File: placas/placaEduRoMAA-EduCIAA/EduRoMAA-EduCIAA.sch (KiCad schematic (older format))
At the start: 78 parts, among them J1 DC_IN, J2 Motor_Izq, J3 Motor_Der, J4 Bluetooth, J5 Sonar, J6 DC_OUT, J7 DC_IN, Q1 BC548, Q2 BC548, Q3 BC548, Q4 BC548, Q5 BC548, SW1 SW_Push, SW2 SW_Push, U1 TCRT5000, U2 TCRT5000, U3 TCST1103, U4 LM393, U5 TCST1103, U6 L293D, U7 IRF7105, U8 IRF7105

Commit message: Reorganizo esquematico y uno librerias
Reorganización general, elimino net repetidas y uno las librerias en una sola
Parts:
- BZ1: symbol EduRoMAA-EduCIAA-rescue:Buzzer-ROBUC_v00_D-ROBUC_v02_EduCiAA-rescue -> EduRoMAA-EduCIAA:Buzzer
- C1, C10, C2, C3, C8, C9: symbol EduRoMAA-EduCIAA-rescue:C-ROBUC_v00_D-ROBUC_v02_EduCiAA-rescue -> EduRoMAA-EduCIAA:C
- C11, C14, C4, C6: symbol Device:CP1_Small -> EduRoMAA-EduCIAA:CP1_Small
- C12, C13, C5, C7: symbol EduRoMAA-EduCIAA-rescue:C_Small-ROBUC_v00_D-ROBUC_v02_EduCiAA-rescue -> EduRoMAA-EduCIAA:C_Small
- ConDer1: symbol Connector_Generic:Conn_01x10 -> EduRoMAA-EduCIAA:Conn_01x10
- ConIzq1: symbol Connector_Generic:Conn_01x12 -> EduRoMAA-EduCIAA:Conn_01x12
- D1: symbol EduRoMAA-EduCIAA-rescue:LED-top_lib-ROBUC_v02_EduCiAA-rescue -> EduRoMAA-EduCIAA:LED
- J1, J2, J3, J6, J7: symbol EduRoMAA-EduCIAA-rescue:Conn_01x02-ROBUC_v00_D-ROBUC_v02_EduCiAA-rescue -> EduRoMAA-EduCIAA:Conn_01x02
- J4, J5: symbol Connector_Generic:Conn_01x04 -> EduRoMAA-EduCIAA:Conn_01x04
- Logo_1: symbol EduRoMAA-EduCIAA-rescue:Logo_CIII-ROBUC_v00_D-ROBUC_v02_EduCiAA-rescue -> EduRoMAA-EduCIAA:Logo_CIII
- MH1, MH2, MH3, MH4: symbol EduRoMAA-EduCIAA-rescue:MountingHole-ROBUC_v00_D-ROBUC_v02_EduCiAA-rescue -> EduRoMAA-EduCIAA:MountingHole
- Q1, Q2, Q3, Q4, Q5: symbol Transistor_BJT:BC548 -> EduRoMAA-EduCIAA:BC548
- R1, R10, R11, R12, R13, R14, R15, R16, R17, R18, R19, R2, R20, R21, R22, R23, R24, R25, R26, R3, R31, R32, R33, R4, R5, R6, R7, R8, R9: symbol EduRoMAA-EduCIAA-rescue:R_US-ROBUC_v00_D-ROBUC_v02_EduCiAA-rescue -> EduRoMAA-EduCIAA:R_US
- R27, R28, R29, R30: symbol Device:R_US -> EduRoMAA-EduCIAA:R_US
- SW1, SW2: symbol EduRoMAA-EduCIAA-rescue:SW_Push-top_lib-ROBUC_v02_EduCiAA-rescue -> EduRoMAA-EduCIAA:SW_Push
- U1, U2: symbol EduRoMAA-EduCIAA-rescue:TCRT5000-ROBUC_v00_D-ROBUC_v02_EduCiAA-rescue -> EduRoMAA-EduCIAA:TCRT5000
- U3, U5: symbol EduRoMAA-EduCIAA-rescue:TCST1103-ROBUC_v00_D-ROBUC_v02_EduCiAA-rescue -> EduRoMAA-EduCIAA:TCST1103
- U4: symbol EduRoMAA-EduCIAA-rescue:LM393-ROBUC_v00_D-ROBUC_v02_EduCiAA-rescue -> EduRoMAA-EduCIAA:LM393
- U6: symbol EduRoMAA-EduCIAA-rescue:L293D-top_lib-ROBUC_v02_EduCiAA-rescue -> EduRoMAA-EduCIAA:L293D
- U7, U8: symbol EduRoMAA-EduCIAA-rescue:IRF7105-IRF7105-ROBUC_v02_EduCiAA-rescue -> EduRoMAA-EduCIAA:IRF7105
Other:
- note added: "Bocina\n\n"
- note added: "Sensores IR\n"
- note added: "Tacómetros"
- note removed: "Buzzer\n\n"
- note removed: "Encoder\n"
- note removed: "Seguidor de linea\n"
- moved on the sheet: C1, C10, C13, C14, C2, C4, C6, C7, C9, ConDer1, ConIzq1, D1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

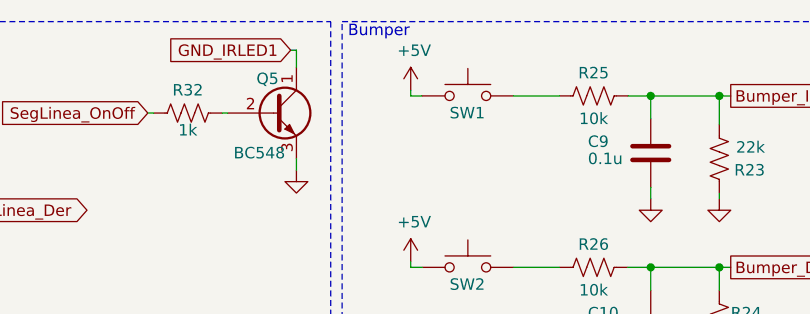
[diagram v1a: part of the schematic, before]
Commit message: [PCB] Modifico serigrafia y re-ruteo.
Modifico serigrafia y algo de ruteo
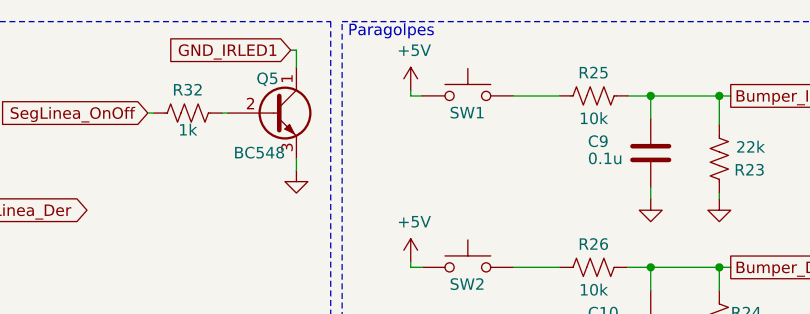
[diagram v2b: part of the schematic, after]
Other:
- note added: "Paragolpes"
- note removed: "Bumper"
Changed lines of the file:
@@
 	550  7150 550  7750
 Text Notes 8800 625  0    50   ~ 0
-Bumper
+Paragolpes
 $Comp
 L EduRoMAA-EduCIAA:SW_Push SW1

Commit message: [PCB] Agrego serigrafia complementaria
Agrego símbolos para serigrafia, lista para revision
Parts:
- added Logo_2: Logo_CIII, lib_fp:Logo_CIII_Small_FSilk, symbol EduRoMAA-EduCIAA:Logo_CIII
- added Logo_3: Logo_ohw, lib_fp:OSHW-Logo_7.5x8mm_SilkScreen, symbol EduRoMAA-EduCIAA:Logo_ohw
- added Logo_4: Logo_KiCad, lib_fp:KiCad-Logo2_8mm_SilkScreen, symbol EduRoMAA-EduCIAA:Logo_KiCad
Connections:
- net labels added: +3.3V
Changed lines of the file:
@@
 	2675 4200 3525 4200
 Wire Notes Line
-	550  7150 2700 7150
-Wire Notes Line
-	2700 7150 2700 7750
-Wire Notes Line
-	2700 7750 550  7750
+	550  7150 4300 7150
+Wire Notes Line
+	4300 7150 4300 7750
+Wire Notes Line
+	4300 7750 550  7750
 Wire Notes Line
 	9275 3825 9275 4425
@@
 Connection ~ 1750 3350
 $Comp
-L EduRoMAA-EduCIAA:+3.3VA #PWR0105
+L EduRoMAA-EduCIAA:+3.3V #PWR0105
 U 1 1 5CC69314
 P 10150 2500
@@
 	8150 3500 8325 3500
 $Comp
-L EduRoMAA-EduCIAA:+3.3VA #PWR0107
-U 1 1 5D0814AC
-P 4575 975
-F 0 "#PWR0107" H 4575 825 50  0001 C CNN
-F 1 "+3.3VA" H 4590 1148 50  0000 C CNN
-F 2 "" H 4575 975 50  0001 C CNN
-F 3 "" H 4575 975 50  0001 C CNN
-	1    4575 975
-	1    0    0    -1
-$EndComp
-$Comp
-L EduRoMAA-EduCIAA:+3.3VA #PWR0113
+L EduRoMAA-EduCIAA:+3.3V #PWR0113
 U 1 1 5D081691
 P 6325 975
@@
 Wire Wire Line
 	8575 675  8550 675
+$Comp
+L EduRoMAA-EduCIAA:Logo_CIII Logo_2
+U 1 1 5D040B7E
+P 2925 7250
+F 0 "Logo_2" H 3132 7224 23  0000 L CNN
+F 1 "Logo_CIII" H 3132 7178 23  0000 L CNN
+F 2 "lib_fp:Logo_CIII_Small_FSilk" H 2925 7250 23  0001 C CNN
+F 3 "" H 2925 7250 23  0001 C CNN
+	1    2925 7250
+	1    0    0    -1
+$EndComp
+$Comp
+L power:+3.3V #PWR0107
+U 1 1 5D0E0863
+P 4575 975
+F 0 "#PWR0107" H 4575 825 50  0001 C CNN
+F 1 "+3.3V" H 4589 1144 50  0000 C CNN
+F 2 "" H 4575 975 50  0001 C CNN
+F 3 "" H 4575 975 50  0001 C CNN
+	1    4575 975
+	1    0    0    -1
+$EndComp
+$Comp
+L EduRoMAA-EduCIAA:Logo_ohw Logo_3
+U 1 1 5D04A910
+P 2950 7575
+F 0 "Logo_3" H 3130 7599 23  0000 L CNN
+F 1 "Logo_ohw" H 3130 7553 23  0000 L CNN
+F 2 "lib_fp:OSHW-Logo_7.5x8mm_SilkScreen" H 2950 7575 50  0001 C CNN
+F 3 "" H 2950 7575 50  0001 C CNN
+	1    2950 7575
+	1    0    0    -1
+$EndComp
+$Comp
+L EduRoMAA-EduCIAA:Logo_KiCad Logo_4
+U 1 1 5D04BCF8
+P 3725 7300
+F 0 "Logo_4" H 4075 7325 23  0000 L CNN
+F 1 "Logo_KiCad" H 4075 7275 23  0000 L CNN
+F 2 "lib_fp:KiCad-Logo2_8mm_SilkScreen" H 3725 7300 50  0001 C CNN
+F 3 "" H 3725 7300 50  0001 C CNN
+	1    3725 7300
+	1    0    0    -1
+$EndComp
 $EndSCHEMATC

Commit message: [PCB] Arreglo teardrops
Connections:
- net labels removed: +3.3VA
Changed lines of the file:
@@
 EESchema Schematic File Version 4
-LIBS:EduRoMAA-EduCIAA-cache
 EELAYER 29 0
 EELAYER END
@@
 P 10150 2500
 F 0 "#PWR0105" H 10150 2350 50  0001 C CNN
-F 1 "+3.3VA" V 10150 2800 50  0000 C CNN
+F 1 "+3.3V" V 10150 2800 50  0000 C CNN
 F 2 "" H 10150 2500 50  0001 C CNN
 F 3 "" H 10150 2500 50  0001 C CNN
@@
 P 6325 975
 F 0 "#PWR0113" H 6325 825 50  0001 C CNN
-F 1 "+3.3VA" H 6340 1148 50  0000 C CNN
+F 1 "+3.3V" H 6340 1148 50  0000 C CNN
 F 2 "" H 6325 975 50  0001 C CNN
 F 3 "" H 6325 975 50  0001 C CNN
